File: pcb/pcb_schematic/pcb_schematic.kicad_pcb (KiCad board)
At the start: 4 copper layers, 41.5 x 48.4 mm, 33 parts, among them J1 Conn_ST_STDC14, J3 Conn_02x02_Odd_Even, J4 USB_B_Micro, Q1 MMBT3904, Q2 MMBT3904, Q3 MMBT3904, U1 STM32G031K8Tx, U2 NCP1117-3.3_SOT223, U4 SSD1306 128 x 64 OLED (0x3C), U5 TCS34725 (0x29), Y1 Crystal

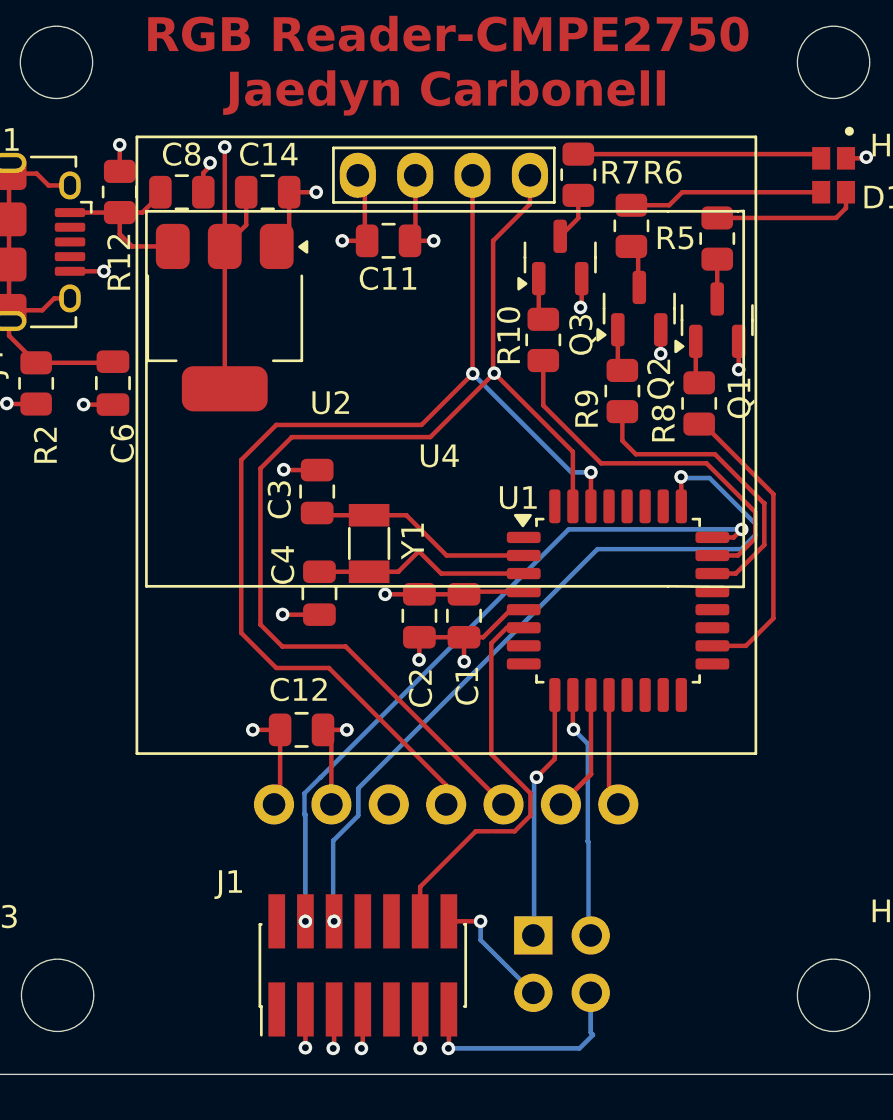
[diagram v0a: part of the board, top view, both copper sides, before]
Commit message: fixerd some warnings with the silkscreen
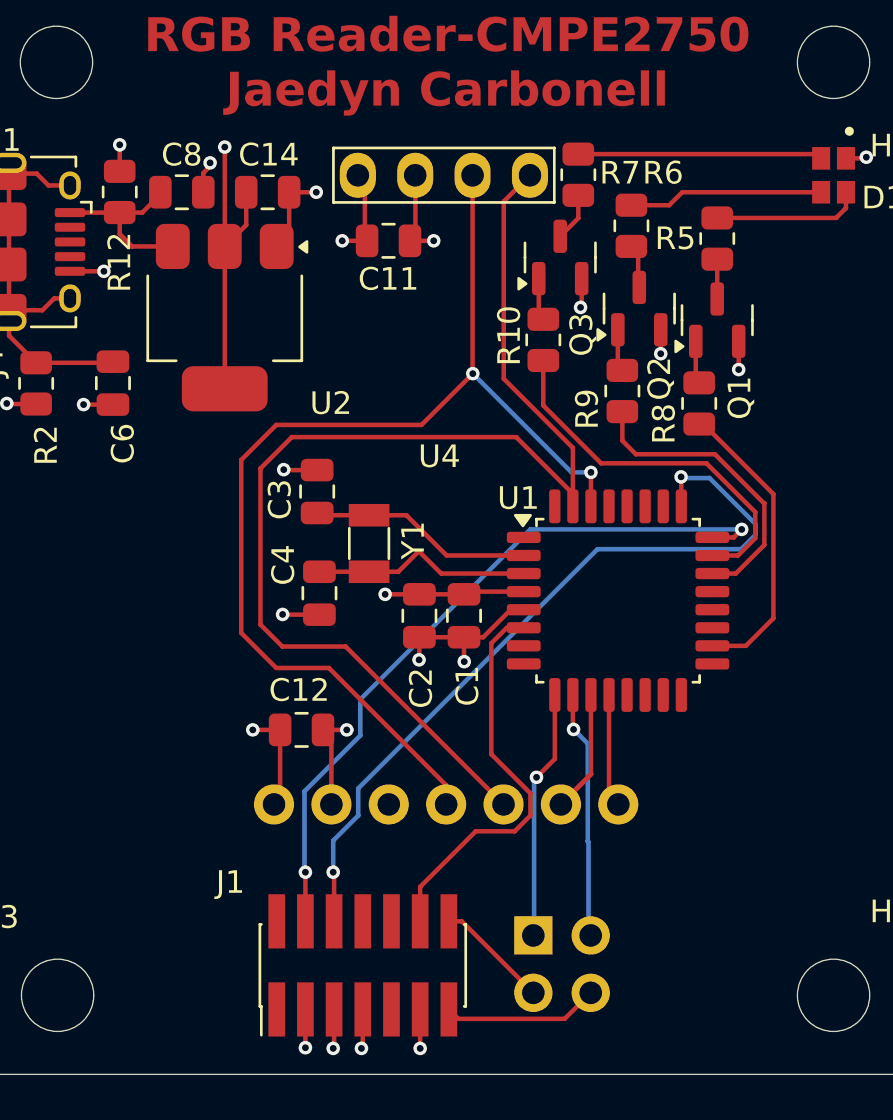
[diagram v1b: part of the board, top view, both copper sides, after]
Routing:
- net SDA: track 49.9 -> 53.4 mm, vias 1 -> 0
- net Net-(J1-VCP_RX): track 10.3 -> 6.93 mm, vias 1 -> 0
- net Net-(J1-JTMS/SWDIO): track 31.6 -> 32.5 mm
- net Net-(J1-VCP_TX): track 5.54 -> 5.05 mm, vias 2 -> 0

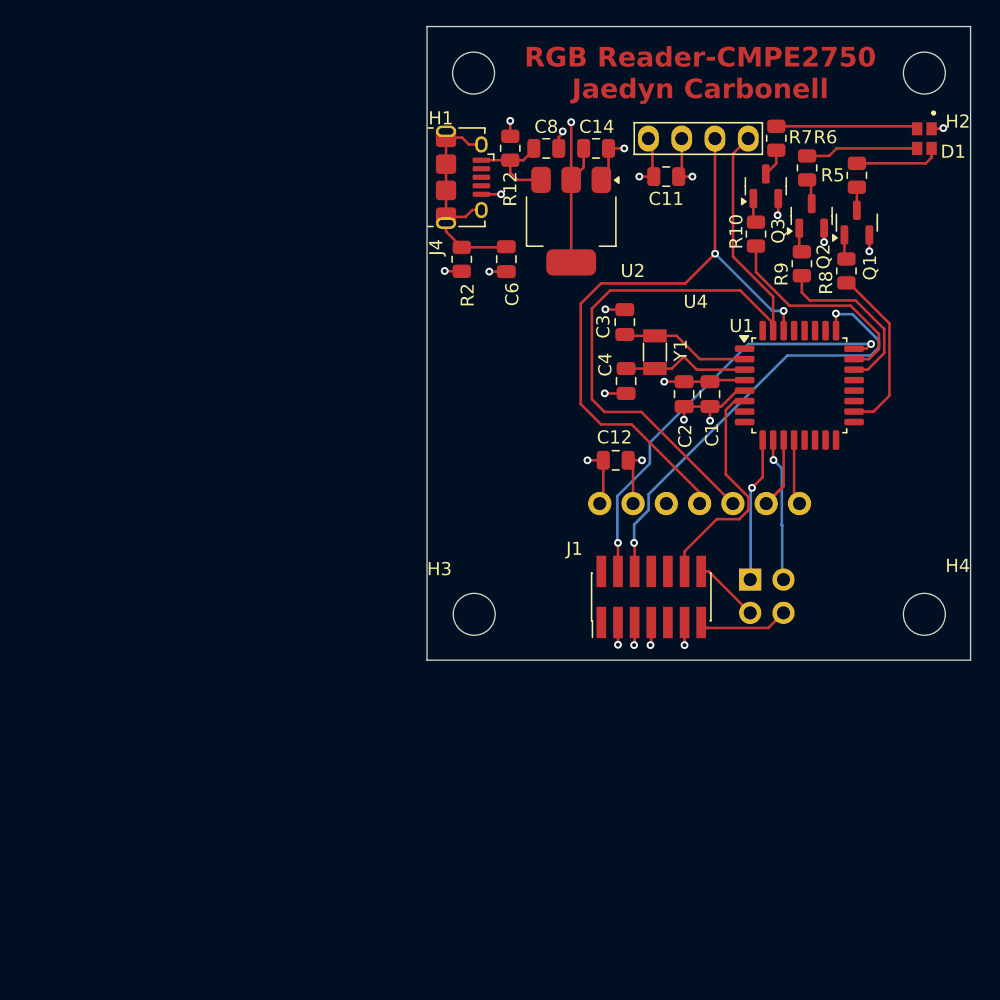
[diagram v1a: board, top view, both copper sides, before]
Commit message: Fixed according to feedback
Schematic -> looks like the current limiting resistors for the read and blue LEDs are reversed.

Bypass caps for the MCU are drawn really weird!

Looks like you moved the XTAL and now you have two redundant wires.

PCB -> Identification is in the copper layer, not the silk layer.

C12 does not need vias, the through-hole header serves as vias.

You've got a split on the SDA line of the MCU - try to route from a via, or another pad if you can.

For the power supply, you've not used the filter caps correctly. Go from the USB connector to C8, then to regulator pin 3 (not from reg pin3 to the usb). You can put a fat track between the two pin 2s. You can add a new via size (1mm, 0.8mm) in the via drop-down, and use these vias for punching into the power planes from the caps. The regulator itself should not punch into the power plane, just it's caps should.
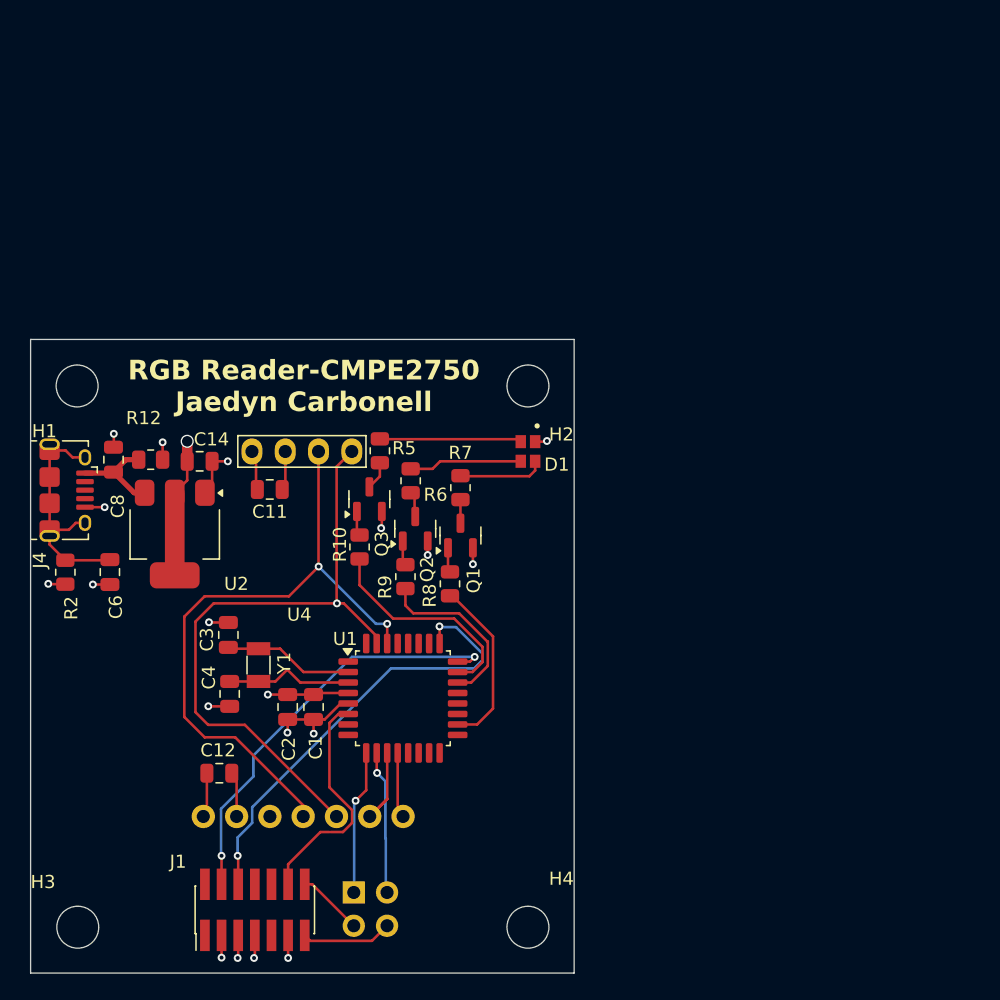
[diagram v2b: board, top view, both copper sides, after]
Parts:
- moved R5 42.0 mm to (147.3, 103.0)
- moved C8 40.7 mm to (127.0, 103.7), turned to -90 degrees
- moved R2 38.5 mm to (123.3, 112.2)
- moved J3 38.5 mm to (145.3, 136.7)
- moved C1 38.5 mm to (142.2, 122.5)
- moved C11 38.5 mm to (138.9, 105.9)
- moved C12 38.5 mm to (135.1, 127.6)
- moved C14 38.5 mm to (133.6, 103.8)
- moved C2 38.5 mm to (140.3, 122.5)
- moved C3 38.5 mm to (135.7, 117.0)
- moved C4 38.5 mm to (135.8, 121.5)
- moved D1 38.5 mm to (158.6, 103.0)
- moved H2 38.5 mm to (158.6, 98.0)
- moved J1 38.5 mm to (137.8, 138.0)
- moved J4 38.5 mm to (123.4, 106.0)
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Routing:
- net +3.3V: track 30.9 -> 25.9 mm, vias 6 -> 4
- net SDA: track 53.4 -> 49.0 mm, vias 0 -> 1
- net GND: track 39.1 -> 36.2 mm, vias 18 -> 16
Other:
- board size 41.5 x 48.4 mm -> 41.5 x 48.3 mm

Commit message: Update pcb_schematic.kicad_pcb
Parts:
- turned C6 to 90 degrees
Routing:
- net Net-(J4-Shield): track 18.0 -> 19.3 mm, vias 0 -> 1
- net GND: track 36.2 -> 34.9 mm, vias 16 -> 15
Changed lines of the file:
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@@
 			(at -2.65 -3.45 0)
 			(layer "F.SilkS")
+			(hide yes)
 			(effects
 				(font
@@
 			(at -2.5 3.45 0)
 			(layer "F.SilkS")
+			(hide yes)
 			(effects
 				(font
@@
 	(footprint "Capacitor_SMD:C_0805_2012Metric"
 		(layer "F.Cu")
-		(at 126.7 112.225 -90)
+		(at 126.7 112.225 90)
 		(descr "Capacitor SMD 0805 (2012 Metric), square (rectangular) end terminal, IPC-7351 nominal, (Body size source: IPC-SM-782 page 76, https://www.pcb-3d.com/wordpress/wp-content/uploads/ipc-sm-782a_amendment_1_and_2.pdf, https://docs.google.com/spreadsheets/d/1BsfQQcO9C6DZCsRaXUlFlo91Tg2WpOkGARC1WS5S8t0/edit?usp=sharing), generated with kicad-footprint-generator")
 		(tags "capacitor")
@@
 		(attr smd)
 		(fp_line
-			(start -0.261252 0.735)
-			(end 0.261252 0.735)
+			(start -0.261252 -0.735)
+			(end 0.261252 -0.735)
 			(stroke
 				(width 0.12)
@@
 		)
 		(fp_line
-			(start -0.261252 -0.735)
-			(end 0.261252 -0.735)
+			(start -0.261252 0.735)
+			(end 0.261252 0.735)
 			(stroke
 				(width 0.12)
@@
 		)
 		(fp_line
-			(start -1.7 0.98)
-			(end -1.7 -0.98)
+			(start 1.7 -0.98)
+			(end 1.7 0.98)
 			(stroke
 				(width 0.05)
@@
 		)
 		(fp_line
-			(start 1.7 0.98)
-			(end -1.7 0.98)
+			(start -1.7 -0.98)
+			(end 1.7 -0.98)
 			(stroke
 				(width 0.05)
@@
 		)
 		(fp_line
-			(start -1.7 -0.98)
-			(end 1.7 -0.98)
+			(start 1.7 0.98)
+			(end -1.7 0.98)
 			(stroke
 				(width 0.05)
@@
 		)
 		(fp_line
-			(start 1.7 -0.98)
-			(end 1.7 0.98)
+			(start -1.7 0.98)
+			(end -1.7 -0.98)
 			(stroke
 				(width 0.05)
@@
 		)
 		(fp_line
-			(start -1 0.625)
-			(end -1 -0.625)
+			(start 1 -0.625)
+			(end 1 0.625)
 			(stroke
 				(width 0.1)
@@
 		)
 		(fp_line
-			(start 1 0.625)
-			(end -1 0.625)
+			(start -1 -0.625)
+			(end 1 -0.625)
 			(stroke
 				(width 0.1)
@@
 		)
 		(fp_line
-			(start -1 -0.625)
-			(end 1 -0.625)
+			(start 1 0.625)
+			(end -1 0.625)
 			(stroke
 				(width 0.1)
@@
 		)
 		(fp_line
-			(start 1 -0.625)
-			(end 1 0.625)
+			(start -1 0.625)
+			(end -1 -0.625)
 			(stroke
 				(width 0.1)
@@
 		)
 		(pad "1" smd roundrect
-			(at -0.95 0 270)
+			(at -0.95 0 90)
 			(size 1 1.45)
 			(layers "F.Cu" "F.Mask" "F.Paste")
@@
 		)
 		(pad "2" smd roundrect
-			(at 0.95 0 270)
+			(at 0.95 0 90)
 			(size 1 1.45)
 			(layers "F.Cu" "F.Mask" "F.Paste")
@@
 			(at 2.55 3.7 0)
 			(layer "F.SilkS")
+			(hide yes)
 			(effects
 				(font
@@
 		(tags "SMD SMT Crystal")
 		(property "Reference" "Y1"
-			(at 0.1492 1.9598 90)
+			(at 2.6742 -0.0402 180)
 			(layer "F.SilkS")
 			(effects
@@
 			(at 2.55 -3.7 0)
 			(layer "F.SilkS")
+			(hide yes)
 			(effects
 				(font
@@
 		(tags "Through hole pin header THT 2x02 2.54mm double row")
 		(property "Reference" "J3"
-			(at -1.15 -5.34 180)
+			(at -1.15 -5.34 0)
 			(layer "B.SilkS")
 			(effects
@@
 		(sheetname "/")
 		(sheetfile "pcb_schematic.kicad_sch")
-		(attr through_hole)
+		(attr through_hole dnp)
 		(fp_line
 			(start -1.38 1.38)
@@
 		(sheetname "/")
 		(sheetfile "pcb_schematic.kicad_sch")
-		(attr smd)
+		(attr smd dnp)
 		(fp_rect
 			(start -8.75 -18.325)
@@
 		(net 1)
 	)
-	(segment
-		(start 126.7 113.175)
-		(end 125.4 113.175)
-		(width 0.2)
-		(layer "F.Cu")
-		(net 1)
-	)
 	(via
 		(at 135.7 103.775)
@@
 	)
 	(via
-		(at 125.4 113.175)
-		(size 0.6)
-		(drill 0.3)
-		(layers "F.Cu" "B.Cu")
-		(net 1)
-	)
-	(via
 		(at 130.725 102.325)
 		(size 0.6)
@@
 		(net 49)
 	)
+	(segment
+		(start 126.7 113.175)
+		(end 125.4 113.175)
+		(width 0.2)
+		(layer "F.Cu")
+		(net 49)
+	)
+	(via
+		(at 125.4 113.175)
+		(size 0.6)
+		(drill 0.3)
+		(layers "F.Cu" "B.Cu")
+		(net 49)
+	)

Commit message: Update pcb_schematic.kicad_pcb
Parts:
- moved R2 5.57 mm to (128.8, 112.8)
- moved C6 3.63 mm to (128.8, 109.3)
- moved U2 1.85 mm to (133.5, 109.3)
- moved R12 1.65 mm to (131.4, 103.2), turned to -90 degrees
- moved C14 0.56 mm to (134.1, 103.8)
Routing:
- net VBUS: track 7.59 -> 12.1 mm
- net +3.3V: track 25.9 -> 23.1 mm
- net GND: track 34.9 -> 35.4 mm, vias 15 -> 16
- net Net-(J4-Shield): track 19.3 -> 19.6 mm, vias 1 -> 0

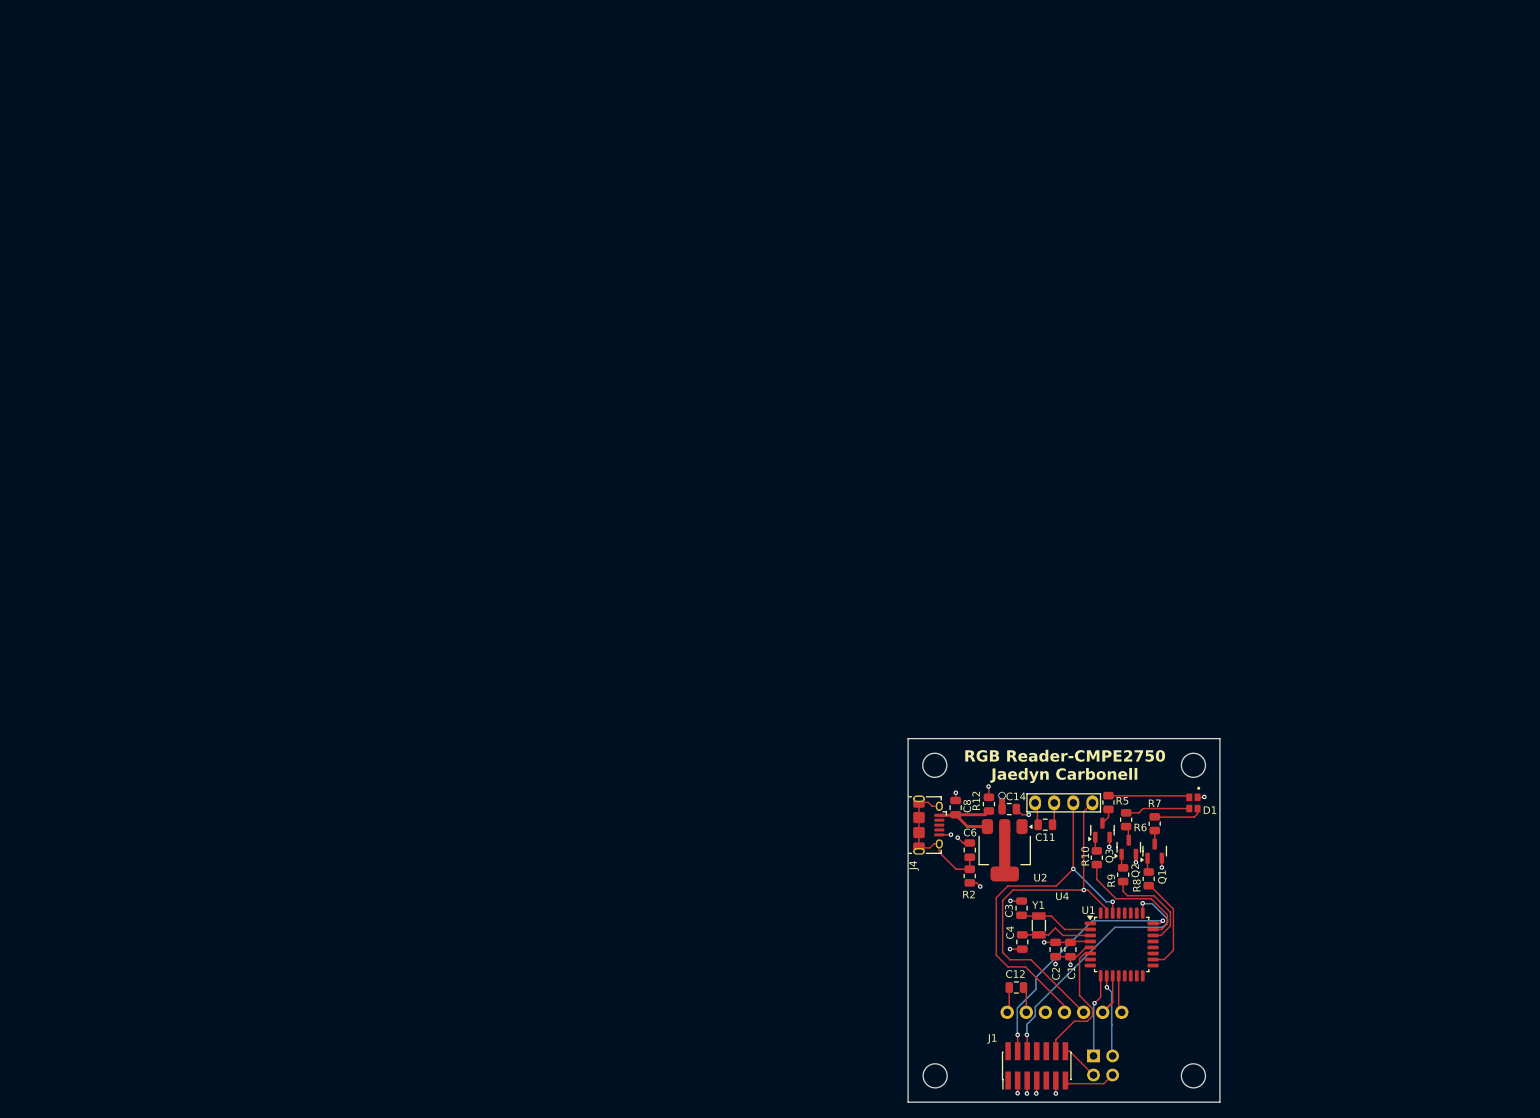
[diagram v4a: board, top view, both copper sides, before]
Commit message: via error
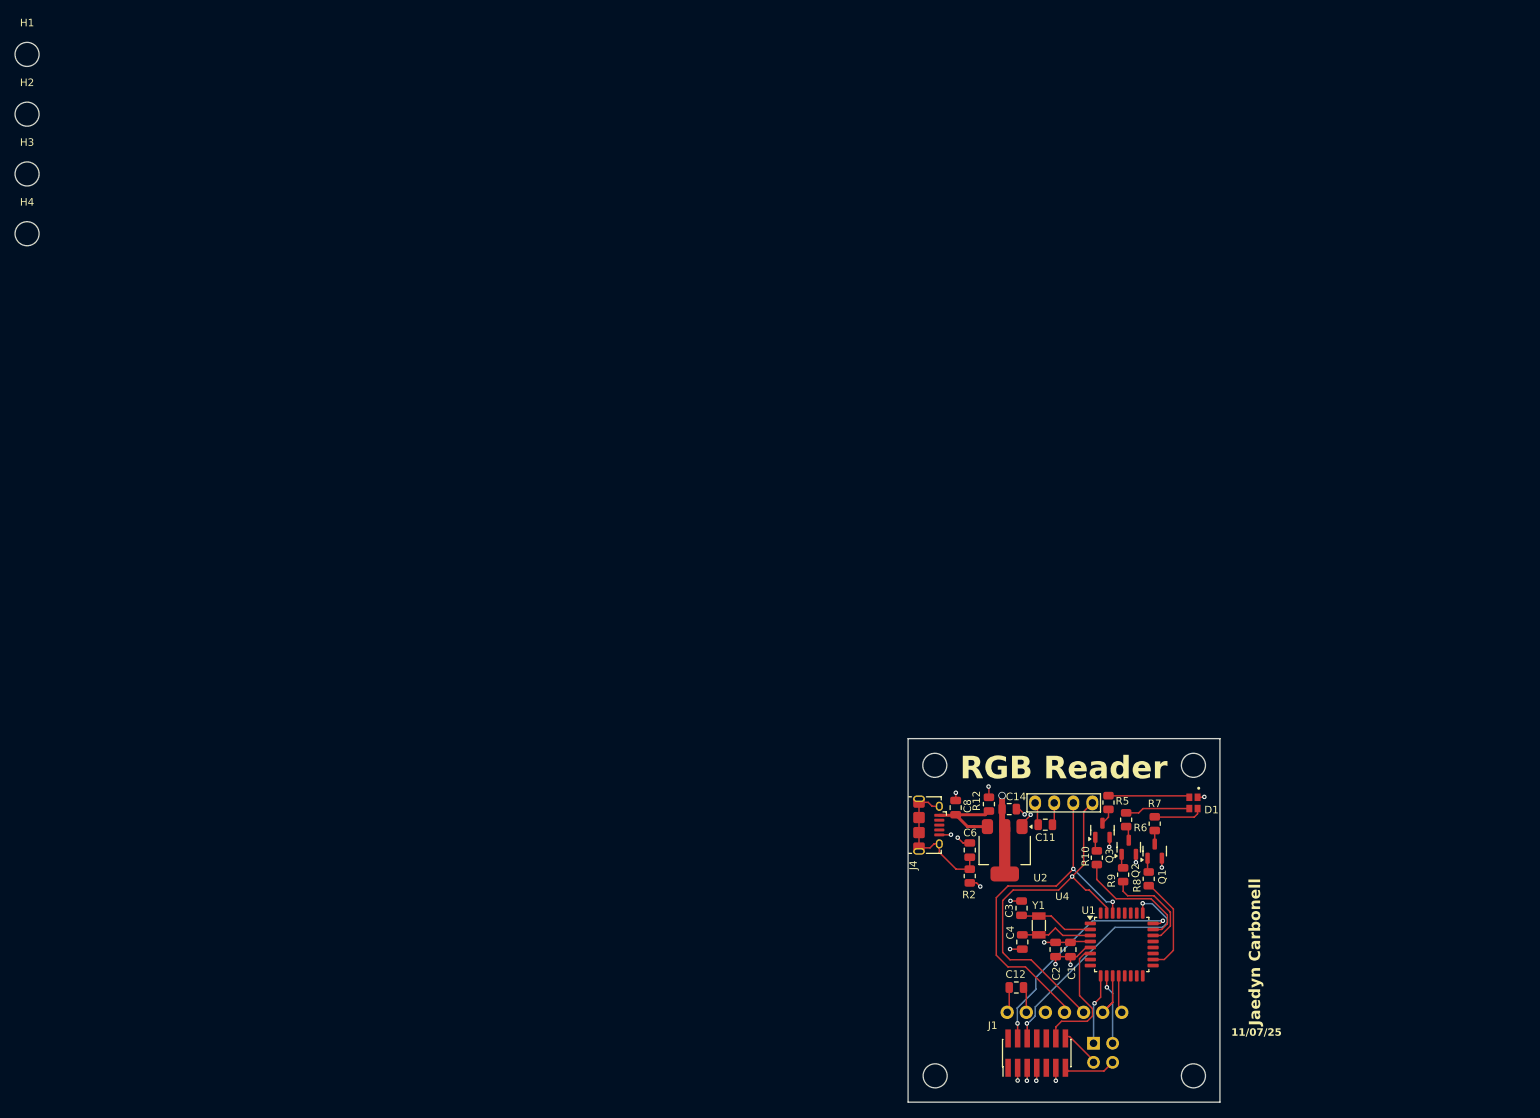
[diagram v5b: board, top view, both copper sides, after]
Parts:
- added H1: MountingHole, MountingHole:MountingHole_3.2mm_M3, F.Cu at (3.48, 3.48)
- added H2: MountingHole, MountingHole:MountingHole_3.2mm_M3, F.Cu at (3.48, 11.4)
- added H3: MountingHole, MountingHole:MountingHole_3.2mm_M3, F.Cu at (3.48, 19.4)
- added H4: MountingHole, MountingHole:MountingHole_3.2mm_M3, F.Cu at (3.48, 27.3)
- moved J1 1.70 mm to (137.8, 136.3)
- moved J3 1.68 mm to (145.3, 135.0)
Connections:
- R5 pad 1: Net-(D1-Pad2) -> Net-(D1-Pad4)
- R5 pad 2: Net-(Q1-C) -> Net-(Q3-C)
- R7 pad 1: Net-(D1-Pad4) -> Net-(D1-Pad2)
- R7 pad 2: Net-(Q3-C) -> Net-(Q1-C)
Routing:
- net Net-(J1-JCLK/SWCLK): track 34.7 -> 32.9 mm
- net Net-(J1-JTMS/SWDIO): track 32.5 -> 30.8 mm
- net Net-(J3-Pin_1): track 11.1 -> 9.51 mm
- net +3.3V: track 23.1 -> 24.6 mm
- net Net-(J3-Pin_3): track 11.1 -> 9.63 mm
- net GND: track 35.4 -> 36.8 mm, vias 16 -> 17
- net Net-(J1-~{RST}): track 18.2 -> 17.5 mm
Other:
- board text added: "11/07/25"
- board text added: "Jaedyn Carbonell"
- board text added: "RGB Reader"
- board text removed: "RGB Reader-CMPE2750 Jaedyn Carbonell"
